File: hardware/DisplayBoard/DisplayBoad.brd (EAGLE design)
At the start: 100 x 54.6 mm, 45 parts, among them IC1 MCP23017, SW1 EC12E_SW, SW2 EC12E_SW, U1 EADOGL128-6

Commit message: Updates
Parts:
- U1: value EADOGL128-6 -> EADOGL128-62; device ea:EADOGL -> ea:EA_DOGL128-6
- moved C12 55.2 mm to (35.6, 37.3), turned to 270 degrees
- moved C10 13.0 mm to (75.9, 40.4)
- moved C11 13.0 mm to (91.2, 40.4)
- moved R2 13.0 mm to (88.6, 40.4)
- moved R3 13.0 mm to (78.5, 40.4)
- moved R5 13.0 mm to (86.1, 40.4)
- moved R6 13.0 mm to (81.0, 40.4)
- moved SW1 13.0 mm to (83.6, 44.2)
- moved C1 12.7 mm to (37.1, 58.4)
- moved C2 12.7 mm to (54.9, 58.4)
- moved C3 12.7 mm to (57.4, 58.4)
- moved C4 12.7 mm to (59.9, 58.4)
- moved C5 12.7 mm to (62.5, 58.4)
- moved C6 12.7 mm to (65.0, 58.4)
- moved C7 12.7 mm to (39.6, 58.4)
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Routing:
- net GND: track 361.0 -> 386.8 mm, vias 2 -> 6
- net ENC1_T: track 47.7 -> 67.2 mm
- net DISP_S3: track 59.6 -> 41.6 mm
- net I2C_SCL: track 40.1 -> 57.2 mm
- net INT: track 53.1 -> 67.7 mm, vias 3 -> 4
- net GPA7: track 43.0 -> 28.8 mm
- net ENC1_S2: track 36.8 -> 49.2 mm
- net GPA5: track 26.9 -> 15.6 mm
- net I2C_SDA: track 43.8 -> 54.3 mm
- net VCC: track 250.1 -> 260.3 mm, vias 0 -> 4
- net DISP_S1: track 41.7 -> 31.6 mm
- net RESET: track 130.1 -> 120.7 mm
- net MODE: track 73.6 -> 65.6 mm
- net ENC1_S1: track 52.8 -> 60.7 mm
- net GPA4: track 18.4 -> 25.5 mm
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- added copper zone on layer 1, net GND
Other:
- board size 100 x 54.6 mm -> 93.4 x 63.7 mm
- board text added: "05/2013"
- board text added: "peschuster.de"

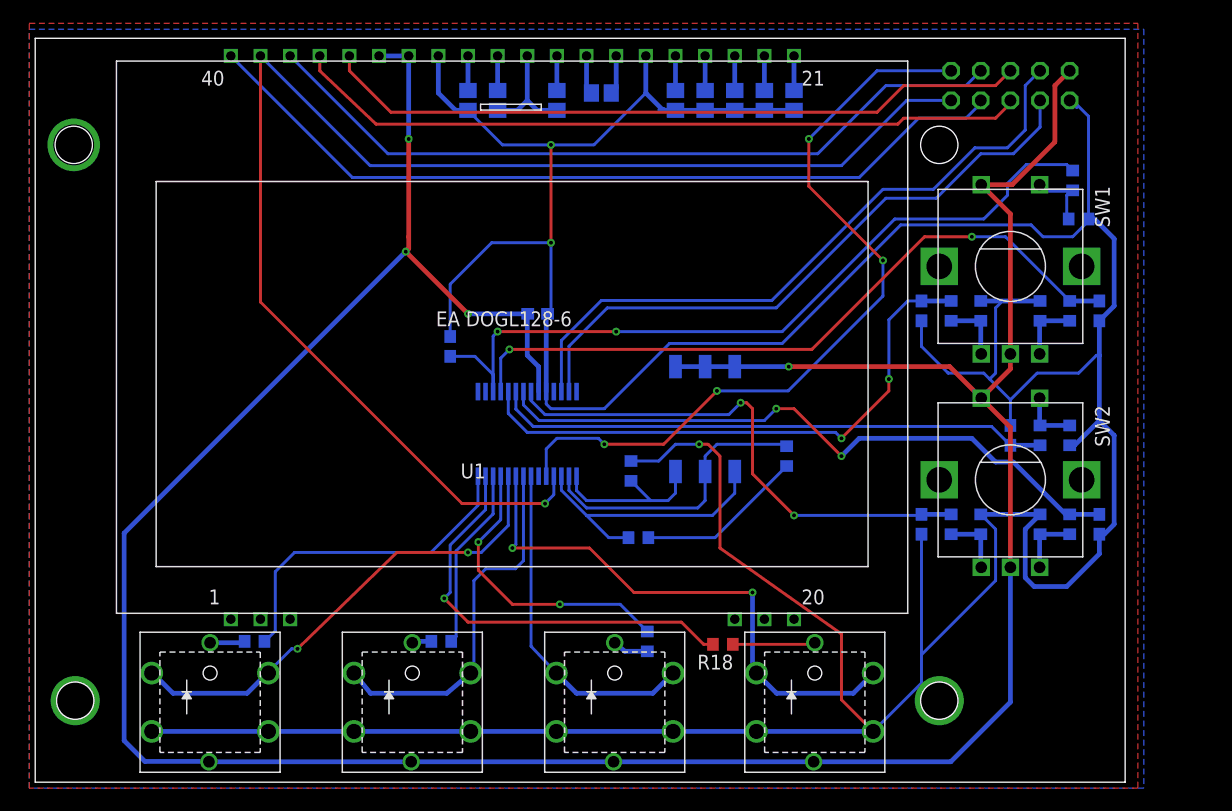
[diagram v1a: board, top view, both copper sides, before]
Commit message: Ordered Version
Small mechanical changes
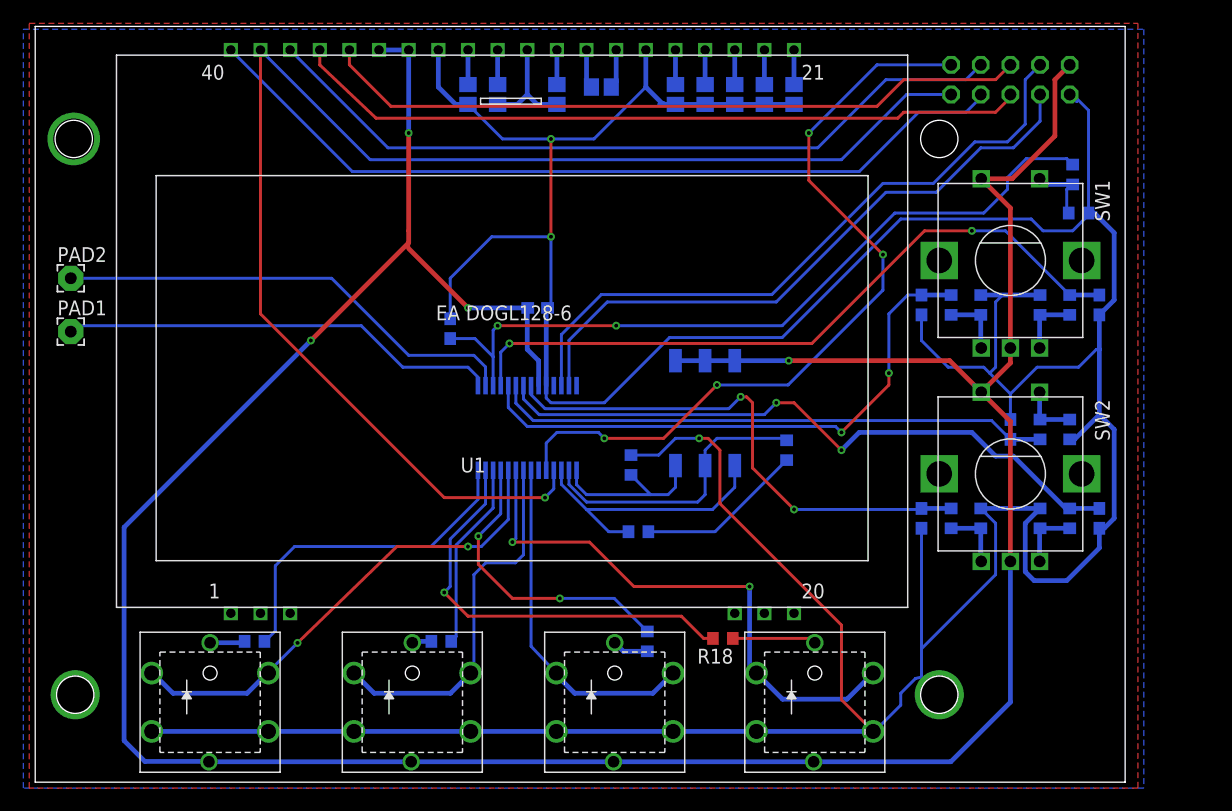
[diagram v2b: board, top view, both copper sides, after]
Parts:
- added PAD1: GPB0, wirepad:2,15/1,0
- added PAD2: GPB1, wirepad:2,15/1,0
- moved C12 1.52 mm to (35.6, 38.9)
- moved C13 0.51 mm to (75.9, 22.6)
- moved C14 0.51 mm to (91.2, 22.6)
- moved C16 0.51 mm to (43.1, 40.6)
- moved C9 0.51 mm to (48.5, 59.6)
- moved IC1 0.51 mm to (42.2, 30.4)
- moved R1 0.51 mm to (88.9, 52.1)
- moved R11 0.51 mm to (86.1, 22.6)
- moved R12 0.51 mm to (81.0, 22.6)
- moved R15 0.51 mm to (51.7, 21.5)
- moved R4 0.51 mm to (89.4, 48.8)
- moved R8 0.51 mm to (88.6, 22.6)
- moved R9 0.51 mm to (78.5, 22.6)
- moved S1 0.51 mm to (57.4, 31.6)
- moved SV1 0.51 mm to (83.6, 60.2)
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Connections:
- net GPB0: now also PAD1.1
- net GPB1: now also PAD2.1
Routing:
- net GPB1: track 0.00 -> 40.3 mm
- net GPB0: track 0.00 -> 37.7 mm
- net ENC1_T: track 67.2 -> 65.7 mm
- net VCC: track 260.3 -> 261.4 mm
- net RESET: track 120.7 -> 121.6 mm
- net DISP_S2: track 46.9 -> 47.8 mm
- net GND: track 386.8 -> 386.0 mm
- net DISP_S1: track 31.6 -> 32.2 mm
- net GPA7: track 28.8 -> 29.3 mm
- net GPA5: track 15.6 -> 16.2 mm
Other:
- board size 93.4 x 63.7 mm -> 93.4 x 64.8 mm

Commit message: DisplayBoard: missing connections
Design error: missing pwr connections for display backlight.
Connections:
- net GND: now also U1.18, U1.19, U1.20
- net VCC: now also U1.1, U1.2, U1.3
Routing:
- net VCC: track 261.4 -> 275.9 mm
- net GND: track 386.0 -> 395.4 mm
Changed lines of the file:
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@@
 <wire x1="57.658" y1="29.464" x2="58.674" y2="28.448" width="0.254" layer="1"/>
 <wire x1="58.674" y1="28.448" x2="58.674" y2="23.876" width="0.254" layer="1"/>
-<wire x1="58.674" y1="23.876" x2="69.088" y2="13.462" width="0.254" layer="1"/>
+<wire x1="58.674" y1="23.876" x2="68.961" y2="13.589" width="0.254" layer="1"/>
+<wire x1="68.961" y1="13.589" x2="69.088" y2="13.462" width="0.254" layer="1"/>
 <wire x1="69.088" y1="13.462" x2="69.088" y2="7.064" width="0.254" layer="1"/>
 <wire x1="69.088" y1="7.064" x2="71.802" y2="4.35" width="0.254" layer="1"/>
@@
 <via x="3.429" y="7.493" extent="1-16" drill="3.2" shape="square"/>
 <via x="77.47" y="7.493" extent="1-16" drill="3.2" shape="square"/>
+<contactref element="U1" pad="18"/>
+<contactref element="U1" pad="19"/>
+<contactref element="U1" pad="20"/>
+<wire x1="59.944" y1="14.478" x2="62.484" y2="14.478" width="0.4064" layer="1"/>
+<wire x1="62.484" y1="14.478" x2="65.024" y2="14.478" width="0.4064" layer="1"/>
+<wire x1="65.024" y1="14.478" x2="68.072" y2="14.478" width="0.4064" layer="1"/>
+<wire x1="68.072" y1="14.478" x2="68.961" y2="13.589" width="0.4064" layer="1"/>
 </signal>
 <signal name="VCC">
@@
 <wire x1="14.986" y1="1.778" x2="9.398" y2="1.778" width="0.4064" layer="16"/>
 <wire x1="9.398" y1="1.778" x2="7.62" y2="3.556" width="0.4064" layer="16"/>
-<wire x1="7.62" y1="3.556" x2="7.62" y2="21.844" width="0.4064" layer="16"/>
+<wire x1="7.62" y1="3.556" x2="7.62" y2="15.24" width="0.4064" layer="16"/>
+<wire x1="7.62" y1="15.24" x2="7.62" y2="21.844" width="0.4064" layer="16"/>
 <wire x1="7.62" y1="21.844" x2="23.622" y2="37.846" width="0.4064" layer="16"/>
 <via x="23.622" y="37.846" extent="1-16" drill="0.3302" shape="octagon"/>
 <wire x1="23.622" y1="37.846" x2="32.004" y2="46.228" width="0.4064" layer="1"/>
 <wire x1="32.004" y1="46.228" x2="32.004" y2="47.244" width="0.4064" layer="1"/>
+<contactref element="U1" pad="1"/>
+<contactref element="U1" pad="2"/>
+<contactref element="U1" pad="3"/>
+<wire x1="21.844" y1="14.478" x2="19.304" y2="14.478" width="0.4064" layer="1"/>
+<wire x1="19.304" y1="14.478" x2="16.764" y2="14.478" width="0.4064" layer="1"/>
+<wire x1="16.764" y1="14.478" x2="8.382" y2="14.478" width="0.4064" layer="16"/>
+<wire x1="8.382" y1="14.478" x2="7.62" y2="15.24" width="0.4064" layer="16"/>
 <wire x1="14.986" y1="1.778" x2="14.886" y2="1.75" width="0" layer="19" extent="16-16"/>
 </signal>
@@
 <wire x1="11.811" y1="7.62" x2="10.081" y2="9.35" width="0.4064" layer="16"/>
 <wire x1="10.081" y1="9.35" x2="9.986" y2="9.35" width="0.4064" layer="16"/>
-<wire x1="20.066" y1="9.525" x2="22.479" y2="11.938" width="0.254" layer="16"/>
-<via x="22.479" y="11.938" extent="1-16" drill="0.3302" shape="octagon"/>
-<wire x1="22.479" y1="11.938" x2="30.988" y2="20.193" width="0.254" layer="1"/>
+<wire x1="20.066" y1="9.525" x2="27.559" y2="17.018" width="0.254" layer="16"/>
+<via x="27.559" y="17.018" extent="1-16" drill="0.3302" shape="octagon"/>
+<wire x1="27.559" y1="17.018" x2="30.988" y2="20.193" width="0.254" layer="1"/>
 <via x="37.084" y="20.193" extent="1-16" drill="0.3302" shape="octagon"/>
 <wire x1="40.539" y1="22.505" x2="40.539" y2="26.728" width="0.254" layer="16"/>
@@
 </signal>
 </signals>
+<errors>
+</errors>
 </board>
 </drawing>
